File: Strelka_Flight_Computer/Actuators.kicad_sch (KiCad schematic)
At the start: 10 parts, among them J3 DB125-3.5-4P-GN-S, J4 SM06B-GHS-TB(LF)(SN)

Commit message: Started design for V2
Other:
- sheet Ematch_Drogue1 ports: added none; removed CONT_TEST
- sheet Ematch_Main ports: added none; removed CONT_TEST
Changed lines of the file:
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@@
   (junction (at 196.85 92.71) (diameter 0) (color 0 0 0 0)
   )
-  (junction (at 64.77 72.39) (diameter 0) (color 0 0 0 0)
-  )
   (junction (at 194.31 95.25) (diameter 0) (color 0 0 0 0)
   )
@@
     (stroke (width 0) (type default))
   )
-  (wire (pts (xy 64.77 72.39) (xy 72.39 72.39))
-    (stroke (width 0) (type default))
-  )
   (wire (pts (xy 186.69 92.71) (xy 189.23 92.71))
     (stroke (width 0) (type default))
@@
     (stroke (width 0) (type default))
   )
-  (wire (pts (xy 64.77 72.39) (xy 64.77 78.74))
-    (stroke (width 0) (type default))
-  )
   (wire (pts (xy 199.39 90.17) (xy 199.39 97.79))
     (stroke (width 0) (type default))
@@
   )
   (wire (pts (xy 163.83 85.09) (xy 168.91 85.09))
-    (stroke (width 0) (type default))
-  )
-  (wire (pts (xy 64.77 67.31) (xy 64.77 72.39))
     (stroke (width 0) (type default))
   )
@@
   )
   (hierarchical_label "DROGUE_CONT" (shape input) (at 101.6 115.57 0) (fields_autoplaced)
-    (effects (font (size 1.27 1.27)) (justify left))
-  )
-  (hierarchical_label "CONT_TEST_EN" (shape input) (at 72.39 72.39 0) (fields_autoplaced)
     (effects (font (size 1.27 1.27)) (justify left))
   )
@@
       (effects (font (size 1.27 1.27)) (justify left top))
     )
-    (pin "CONT_TEST" input (at 64.77 78.74 90)
-      (effects (font (size 1.27 1.27)) (justify right))
-    )
     (pin "EMATCH_Cont" input (at 91.44 115.57 0)
       (effects (font (size 1.27 1.27)) (justify right))
@@
       (effects (font (size 1.27 1.27)) (justify left top))
     )
-    (pin "CONT_TEST" input (at 64.77 67.31 270)
-      (effects (font (size 1.27 1.27)) (justify left))
-    )
     (pin "EMATCH_Cont" input (at 91.44 38.1 0)

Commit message: Routing starting
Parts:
- removed R66, R67, R68: 33, Resistor_SMD:R_0603_1608Metric_Pad0.98x0.95mm_HandSolder, symbol Device:R_Small
- added R18, R19, R21: 33, Resistor_SMD:R_0402_1005Metric, symbol Device:R_Small
- R65: footprint Resistor_SMD:R_0603_1608Metric_Pad0.98x0.95mm_HandSolder -> Resistor_SMD:R_0402_1005Metric; LCSC (none) -> C25105
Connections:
- net EXT_SPI_CS: now also R21.2
- net EXT_SPI_MOSI: now also R18.2
- net EXT_SPI_SCK: now also R19.2
- net at D6.4 (K), J4.3: now also R18.1
- net at D6.1 (K), J4.5: now also R21.1
- net at D6.3 (K), J4.4: now also R19.1
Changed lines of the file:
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@@
     (effects (font (size 1.27 1.27)) (justify left))
-  )
-  (symbol (lib_id "Device:R_Small") (at 191.77 90.17 270) (unit 1)
-    (in_bom yes) (on_board yes) (dnp no)
-    (property "Reference" "R66" (at 189.865 90.17 90)
-      (effects (font (size 1.27 1.27)) (justify right))
-    )
-    (property "Value" "33" (at 193.04 90.17 90)
-      (effects (font (size 1.27 1.27)) (justify right))
-    )
-    (property "Footprint" "Resistor_SMD:R_0603_1608Metric_Pad0.98x0.95mm_HandSolder" (at 191.77 90.17 0)
-      (effects (font (size 1.27 1.27)) hide)
-    )
-    (property "Datasheet" "~" (at 191.77 90.17 0)
-      (effects (font (size 1.27 1.27)) hide)
-    )
-    (pin "1")
-    (pin "2")
-    (instances
-      (project "Strelka_Flight_Computer"
-        (path "/e63e39d7-6ac0-4ffd-8aa3-1841a4541b55/35cf6da3-4352-42df-b1af-73b09ff2e1d9"
-          (reference "R66") (unit 1)
-        )
-      )
-    )
   )
   (symbol (lib_id "Power_Protection:SP0504BAJT") (at 196.85 102.87 0) (unit 1)
@@
     )
   )
+  (symbol (lib_id "Device:R_Small") (at 191.77 95.25 270) (unit 1)
+    (in_bom yes) (on_board yes) (dnp no)
+    (property "Reference" "R21" (at 189.865 95.25 90)
+      (effects (font (size 1.27 1.27)) (justify right))
+    )
+    (property "Value" "33" (at 193.04 95.25 90)
+      (effects (font (size 1.27 1.27)) (justify right))
+    )
+    (property "Footprint" "Resistor_SMD:R_0402_1005Metric" (at 191.77 95.25 0)
+      (effects (font (size 1.27 1.27)) hide)
+    )
+    (property "Datasheet" "~" (at 191.77 95.25 0)
+      (effects (font (size 1.27 1.27)) hide)
+    )
+    (property "LCSC" "C25105" (at 191.77 95.25 90)
+      (effects (font (size 1.27 1.27)) hide)
+    )
+    (pin "1")
+    (pin "2")
+    (instances
+      (project "Strelka_Flight_Computer"
+        (path "/e63e39d7-6ac0-4ffd-8aa3-1841a4541b55/35cf6da3-4352-42df-b1af-73b09ff2e1d9"
+          (reference "R21") (unit 1)
+        )
+      )
+    )
+  )
   (symbol (lib_id "power:GND") (at 161.29 96.52 0) (unit 1)
     (in_bom yes) (on_board yes) (dnp no) (fields_autoplaced)
@@
     )
   )
-  (symbol (lib_id "Device:R_Small") (at 191.77 95.25 270) (unit 1)
-    (in_bom yes) (on_board yes) (dnp no)
-    (property "Reference" "R68" (at 189.865 95.25 90)
-      (effects (font (size 1.27 1.27)) (justify right))
-    )
-    (property "Value" "33" (at 193.04 95.25 90)
-      (effects (font (size 1.27 1.27)) (justify right))
-    )
-    (property "Footprint" "Resistor_SMD:R_0603_1608Metric_Pad0.98x0.95mm_HandSolder" (at 191.77 95.25 0)
-      (effects (font (size 1.27 1.27)) hide)
-    )
-    (property "Datasheet" "~" (at 191.77 95.25 0)
-      (effects (font (size 1.27 1.27)) hide)
-    )
-    (pin "1")
-    (pin "2")
-    (instances
-      (project "Strelka_Flight_Computer"
-        (path "/e63e39d7-6ac0-4ffd-8aa3-1841a4541b55/35cf6da3-4352-42df-b1af-73b09ff2e1d9"
-          (reference "R68") (unit 1)
+  (symbol (lib_id "Device:R_Small") (at 191.77 92.71 270) (unit 1)
+    (in_bom yes) (on_board yes) (dnp no)
+    (property "Reference" "R19" (at 189.865 92.71 90)
+      (effects (font (size 1.27 1.27)) (justify right))
+    )
+    (property "Value" "33" (at 193.04 92.71 90)
+      (effects (font (size 1.27 1.27)) (justify right))
+    )
+    (property "Footprint" "Resistor_SMD:R_0402_1005Metric" (at 191.77 92.71 0)
+      (effects (font (size 1.27 1.27)) hide)
+    )
+    (property "Datasheet" "~" (at 191.77 92.71 0)
+      (effects (font (size 1.27 1.27)) hide)
+    )
+    (property "LCSC" "C25105" (at 191.77 92.71 90)
+      (effects (font (size 1.27 1.27)) hide)
+    )
+    (pin "1")
+    (pin "2")
+    (instances
+      (project "Strelka_Flight_Computer"
+        (path "/e63e39d7-6ac0-4ffd-8aa3-1841a4541b55/35cf6da3-4352-42df-b1af-73b09ff2e1d9"
+          (reference "R19") (unit 1)
         )
       )
@@
   )
   (symbol (lib_id "SM06B-GHS-TB_LF__SN_:SM06B-GHS-TB(LF)(SN)") (at 236.22 92.71 0) (unit 1)
-    (in_bom yes) (on_board yes) (dnp no) (fields_autoplaced)
+    (in_bom yes) (on_board yes) (dnp no)
     (property "Reference" "J4" (at 242.062 93.1453 0)
       (effects (font (size 1.27 1.27)) (justify left))
@@
     )
   )
-  (symbol (lib_id "Device:R_Small") (at 191.77 92.71 270) (unit 1)
-    (in_bom yes) (on_board yes) (dnp no)
-    (property "Reference" "R67" (at 189.865 92.71 90)
-      (effects (font (size 1.27 1.27)) (justify right))
-    )
-    (property "Value" "33" (at 193.04 92.71 90)
-      (effects (font (size 1.27 1.27)) (justify right))
-    )
-    (property "Footprint" "Resistor_SMD:R_0603_1608Metric_Pad0.98x0.95mm_HandSolder" (at 191.77 92.71 0)
-      (effects (font (size 1.27 1.27)) hide)
-    )
-    (property "Datasheet" "~" (at 191.77 92.71 0)
-      (effects (font (size 1.27 1.27)) hide)
-    )
-    (pin "1")
-    (pin "2")
-    (instances
-      (project "Strelka_Flight_Computer"
-        (path "/e63e39d7-6ac0-4ffd-8aa3-1841a4541b55/35cf6da3-4352-42df-b1af-73b09ff2e1d9"
-          (reference "R67") (unit 1)
-        )
-      )
-    )
-  )
   (symbol (lib_id "power:GND") (at 220.98 104.14 0) (unit 1)
     (in_bom yes) (on_board yes) (dnp no) (fields_autoplaced)
@@
       (effects (font (size 1.27 1.27)) (justify right))
     )
-    (property "Footprint" "Resistor_SMD:R_0603_1608Metric_Pad0.98x0.95mm_HandSolder" (at 191.77 87.63 0)
+    (property "Footprint" "Resistor_SMD:R_0402_1005Metric" (at 191.77 87.63 0)
       (effects (font (size 1.27 1.27)) hide)
     )
     (property "Datasheet" "~" (at 191.77 87.63 0)
+      (effects (font (size 1.27 1.27)) hide)
+    )
+    (property "LCSC" "C25105" (at 191.77 87.63 90)
       (effects (font (size 1.27 1.27)) hide)
     )
@@
         )
       )
+    )
+  )
+  (symbol (lib_id "Device:R_Small") (at 191.77 90.17 270) (unit 1)
+    (in_bom yes) (on_board yes) (dnp no)
+    (property "Reference" "R18" (at 189.865 90.17 90)
+      (effects (font (size 1.27 1.27)) (justify right))
+    )
+    (property "Value" "33" (at 193.04 90.17 90)
+      (effects (font (size 1.27 1.27)) (justify right))
+    )
+    (property "Footprint" "Resistor_SMD:R_0402_1005Metric" (at 191.77 90.17 0)
+      (effects (font (size 1.27 1.27)) hide)
+    )
+    (property "Datasheet" "~" (at 191.77 90.17 0)
+      (effects (font (size 1.27 1.27)) hide)
+    )
+    (property "LCSC" "C25105" (at 191.77 90.17 90)
+      (effects (font (size 1.27 1.27)) hide)
+    )
+    (pin "1")
+    (pin "2")
+    (instances
+      (project "Strelka_Flight_Computer"
+        (path "/e63e39d7-6ac0-4ffd-8aa3-1841a4541b55/35cf6da3-4352-42df-b1af-73b09ff2e1d9"
+          (reference "R18") (unit 1)
+        )
+      )

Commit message: Routing complete
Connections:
- net Ematch_Drogue1/EMATCH+ renamed D+
- net Ematch_Drogue1/EMATCH- renamed D-
- net Ematch_Main/EMATCH+ renamed M+
- net Ematch_Main/EMATCH- renamed M-
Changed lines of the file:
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@@
     (effects (font (size 1.27 1.27)) (justify right bottom))
+  )
+  (label "D+" (at 95.377 83.82 0) (fields_autoplaced)
+    (effects (font (size 1.27 1.27)) (justify left bottom))
+  )
+  (label "M-" (at 95.377 62.865 0) (fields_autoplaced)
+    (effects (font (size 1.27 1.27)) (justify left bottom))
+  )
+  (label "M+" (at 95.377 64.77 0) (fields_autoplaced)
+    (effects (font (size 1.27 1.27)) (justify left bottom))
+  )
+  (label "D-" (at 95.377 81.915 0) (fields_autoplaced)
+    (effects (font (size 1.27 1.27)) (justify left bottom))
   )
   (hierarchical_label "MAIN_CONT" (shape input) (at 101.6 38.1 0) (fields_autoplaced)

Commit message: Created BOM
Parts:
- D6: LCSC (none) -> C5116451; LCSC# C5116451 -> (none)
- FB2: LCSC (none) -> C80165; LCSC# C80165 -> (none)
- J3: LCSC (none) -> C2757925; LCSC# C2757925 -> (none)
- J4: LCSC (none) -> C133065; LCSC# C133065 -> (none)
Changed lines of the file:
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@@
       (effects (font (size 1.27 1.27)) hide)
     )
-    (property "LCSC#" "C5116451" (at 196.85 102.87 0)
+    (property "LCSC" "C5116451" (at 196.85 102.87 0)
       (effects (font (size 1.27 1.27)) hide)
     )
@@
       (effects (font (size 1.27 1.27)) (justify left bottom) hide)
     )
-    (property "LCSC#" "C133065" (at 236.22 92.71 0)
+    (property "LCSC" "C133065" (at 236.22 92.71 0)
       (effects (font (size 1.27 1.27)) (justify left bottom) hide)
     )
@@
       (effects (font (size 1.27 1.27)) hide)
     )
-    (property "LCSC#" "C2757925" (at 119.38 72.39 0)
+    (property "LCSC" "C2757925" (at 119.38 72.39 0)
       (effects (font (size 1.27 1.27)) hide)
     )
@@
       (effects (font (size 1.27 1.27)) hide)
     )
-    (property "LCSC#" "C80165" (at 161.29 85.09 90)
-      (effects (font (size 1.27 1.27)) hide)
-    )
+    (property "LCSC" "C80165" (at 161.29 85.09 90)
+      (effects (font (size 1.27 1.27)) hide)
+    )

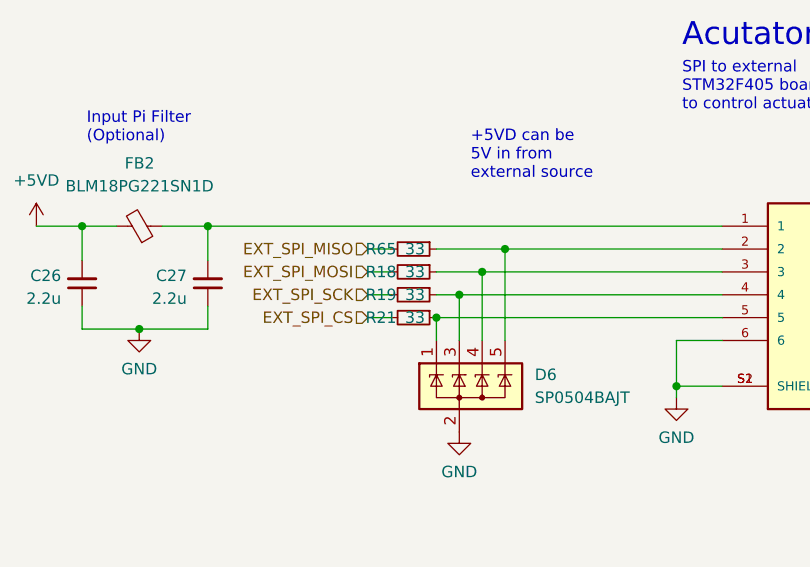
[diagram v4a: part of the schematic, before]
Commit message: Added LCSC mpn to all relevent parts
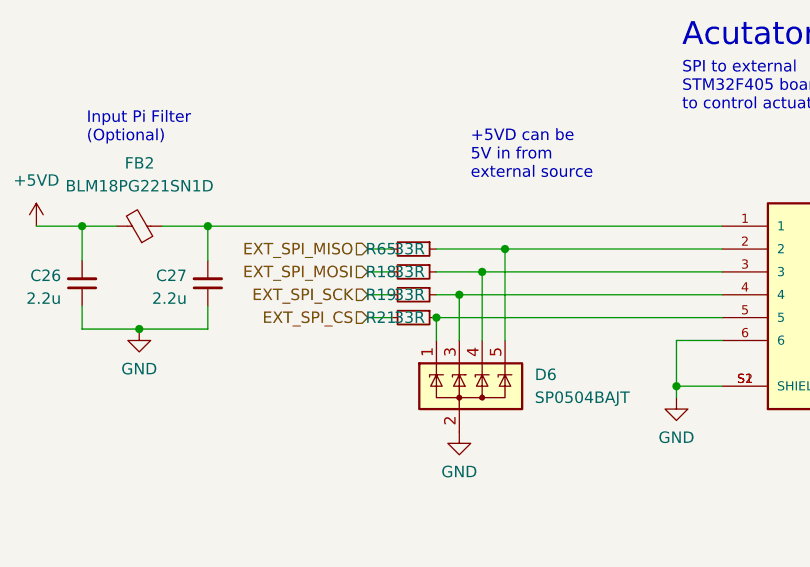
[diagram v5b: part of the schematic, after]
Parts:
- C26, C27: LCSC (none) -> C23630
- R18, R19, R21, R65: value 33 -> 33R
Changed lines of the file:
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@@
       (effects (font (size 1.27 1.27)) (justify right))
     )
-    (property "Value" "33" (at 193.04 95.25 90)
+    (property "Value" "33R" (at 193.04 95.25 90)
       (effects (font (size 1.27 1.27)) (justify right))
     )
@@
       (effects (font (size 1.27 1.27)) (justify right))
     )
-    (property "Value" "33" (at 193.04 92.71 90)
+    (property "Value" "33R" (at 193.04 92.71 90)
       (effects (font (size 1.27 1.27)) (justify right))
     )
@@
       (effects (font (size 1.27 1.27)) (justify right))
     )
-    (property "Value" "33" (at 193.04 87.63 90)
+    (property "Value" "33R" (at 193.04 87.63 90)
       (effects (font (size 1.27 1.27)) (justify right))
     )
@@
     )
     (property "Datasheet" "~" (at 154.94 91.44 0)
+      (effects (font (size 1.27 1.27)) hide)
+    )
+    (property "LCSC" "C23630" (at 154.94 91.44 0)
       (effects (font (size 1.27 1.27)) hide)
     )
@@
       (effects (font (size 1.27 1.27)) (justify right))
     )
-    (property "Value" "33" (at 193.04 90.17 90)
+    (property "Value" "33R" (at 193.04 90.17 90)
       (effects (font (size 1.27 1.27)) (justify right))
     )
@@
       (effects (font (size 1.27 1.27)) hide)
     )
+    (property "LCSC" "C23630" (at 168.91 91.44 0)
+      (effects (font (size 1.27 1.27)) hide)
+    )
